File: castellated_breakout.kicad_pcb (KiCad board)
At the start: 2 copper layers, 3 parts, among them J1 Conn_01x14_Female, J2 Conn_01x14_Female, U1 STM32_7x4_Castellated

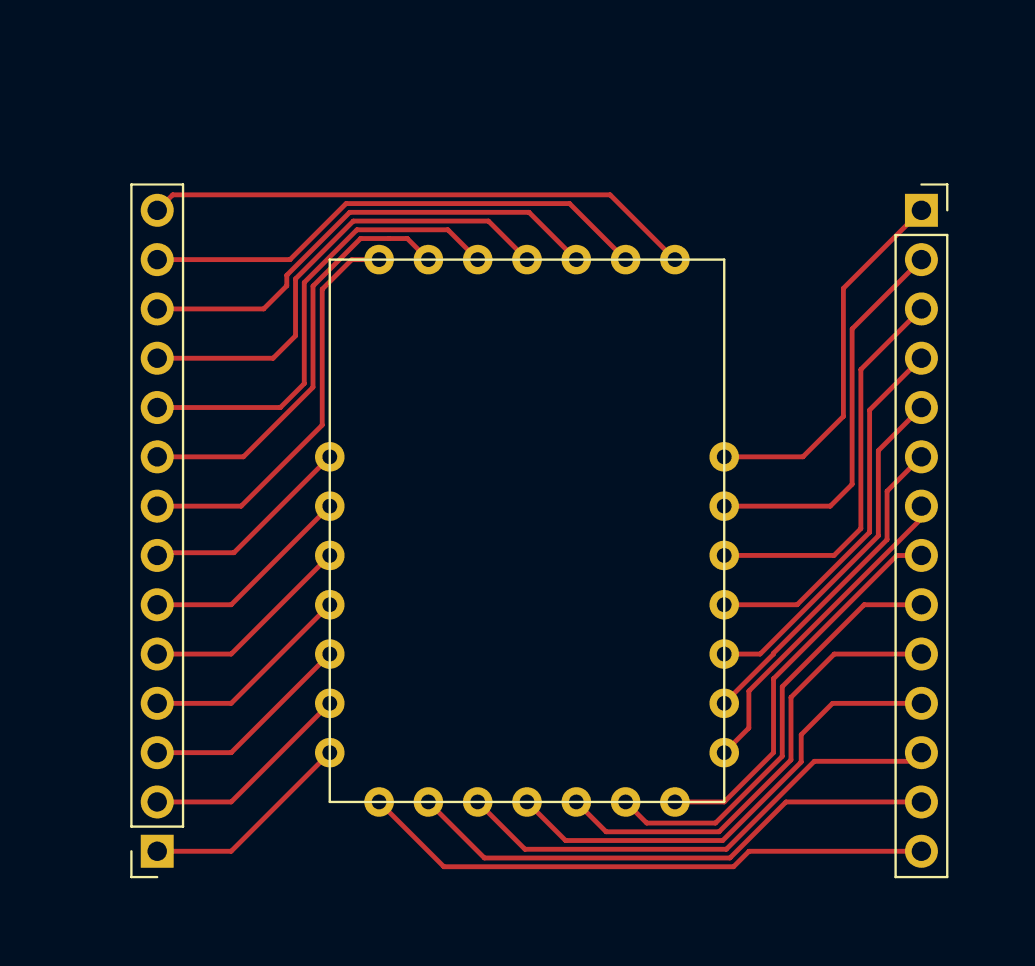
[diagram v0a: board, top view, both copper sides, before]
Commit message: spaced out traces
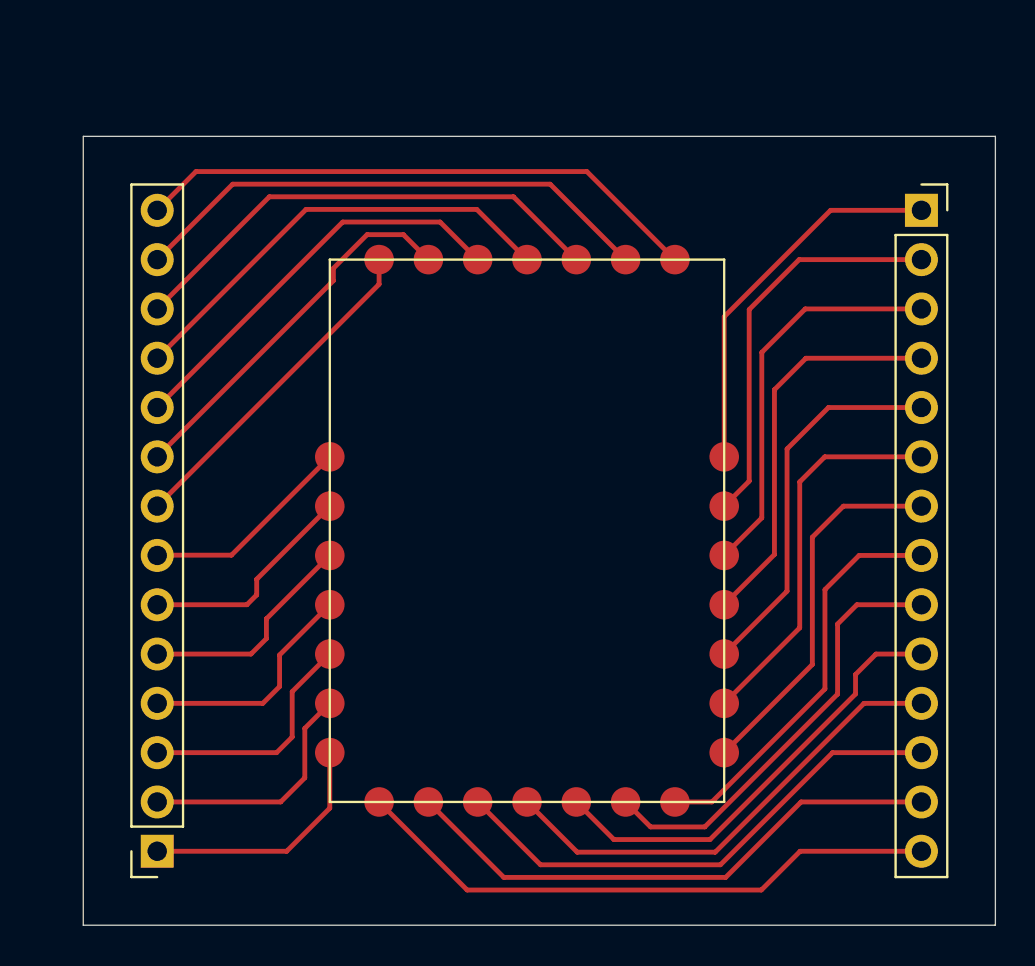
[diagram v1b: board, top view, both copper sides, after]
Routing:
- net Net-(J2-Pad8): track 20.8 -> 17.4 mm
- net Net-(J1-Pad6): track 16.9 -> 19.8 mm
- net Net-(J2-Pad10): track 24.0 -> 21.3 mm
- net Net-(J2-Pad9): track 22.1 -> 19.6 mm
- net Net-(J1-Pad7): track 16.9 -> 19.3 mm
- net Net-(J1-Pad5): track 18.0 -> 19.7 mm
- net Net-(J2-Pad1): track 11.0 -> 12.7 mm
- net Net-(J2-Pad2): track 11.0 -> 12.5 mm
- net Net-(J2-Pad3): track 11.0 -> 12.4 mm
- net Net-(J1-Pad4): track 19.1 -> 20.4 mm
- net Net-(J2-Pad11): track 24.5 -> 23.3 mm
- net Net-(J1-Pad14): track 29.7 -> 30.6 mm
- net Net-(J2-Pad14): track 28.4 -> 29.4 mm
- net Net-(J1-Pad10): track 24.1 -> 23.1 mm
- net Net-(J2-Pad4): track 11.0 -> 11.9 mm
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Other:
- board outline added: 47 x 40.6 mm
- net class Default: clearance 0.2 -> 0.4
- rule trace_clearance: 0.2 -> 0.4

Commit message: gerbers, v1
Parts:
- moved J2 1.91 mm to (137.8, 113.0)
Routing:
- net Net-(J2-Pad7): track 11.0 -> 12.9 mm
- net Net-(J2-Pad9): track 19.6 -> 21.5 mm
- net Net-(J2-Pad8): track 17.4 -> 19.3 mm
- net Net-(J2-Pad6): track 11.5 -> 13.4 mm
- net Net-(J2-Pad5): track 11.6 -> 13.5 mm
- net Net-(J2-Pad4): track 11.9 -> 13.9 mm
- net Net-(J2-Pad3): track 12.4 -> 14.3 mm
- net Net-(J2-Pad2): track 12.5 -> 14.4 mm
- net Net-(J2-Pad14): track 29.4 -> 31.3 mm
- net Net-(J2-Pad13): track 27.4 -> 29.3 mm
- net Net-(J2-Pad12): track 25.3 -> 27.2 mm
- net Net-(J2-Pad11): track 23.3 -> 25.2 mm
- net Net-(J2-Pad10): track 21.3 -> 23.2 mm
- net Net-(J2-Pad1): track 12.7 -> 14.6 mm
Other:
- board size 47 x 40.6 mm -> 48.9 x 40.6 mm
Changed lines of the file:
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@@
   (general
     (thickness 1.6)
-    (drawings 4)
-    (tracks 108)
+    (drawings 6)
+    (tracks 123)
     (zones 0)
     (modules 3)
@@
       (outputformat 1)
       (mirror false)
-      (drillshape 1)
+      (drillshape 0)
       (scaleselection 1)
-      (outputdirectory ""))
+      (outputdirectory "Gerbers/"))
   )
   (net 0 "")
@@
   )
   (module Connector_PinSocket_2.54mm:PinSocket_1x14_P2.54mm_Vertical (layer F.Cu)
-    (at 139.7 113.03 180)
+    (at 137.795 113.03 180)
     (descr "Through hole straight socket strip, 1x14, 2.54mm pitch, single row (from Kicad 4.0.7), script generated")
     (tags "Through hole socket strip THT 1x14 2.54mm single row")
@@
     )
   )
-  (gr_line (start 135.89 116.84) (end 135.89 76.2) (layer Edge.Cuts) (width 0.05))
+  (gr_line (start 133.985 116.84) (end 135.89 116.84) (layer Edge.Cuts) (width 0.05))
+  (gr_line (start 133.985 76.2) (end 135.89 76.2) (layer Edge.Cuts) (width 0.05))
+  (gr_line (start 133.985 116.84) (end 133.985 76.2) (layer Edge.Cuts) (width 0.05))
   (gr_line (start 182.88 116.84) (end 135.89 116.84) (layer Edge.Cuts) (width 0.05))
   (gr_line (start 182.88 76.2) (end 182.88 116.84) (layer Edge.Cuts) (width 0.05))
@@
   (segment (start 161.832949 78.012949) (end 141.697051 78.012949) (width 0.25) (layer F.Cu) (net 15))
   (segment (start 166.37 82.55) (end 161.832949 78.012949) (width 0.25) (layer F.Cu) (net 15))
+  (segment (start 139.7 80.01) (end 137.795 80.01) (width 0.25) (layer F.Cu) (net 15))
   (segment (start 159.942959 78.662959) (end 143.587041 78.662959) (width 0.25) (layer F.Cu) (net 16))
   (segment (start 143.587041 78.662959) (end 139.7 82.55) (width 0.25) (layer F.Cu) (net 16))
   (segment (start 163.83 82.55) (end 159.942959 78.662959) (width 0.25) (layer F.Cu) (net 16))
+  (segment (start 139.7 82.55) (end 137.795 82.55) (width 0.25) (layer F.Cu) (net 16))
   (segment (start 145.477031 79.312969) (end 139.7 85.09) (width 0.25) (layer F.Cu) (net 17))
   (segment (start 158.052969 79.312969) (end 145.477031 79.312969) (width 0.25) (layer F.Cu) (net 17))
   (segment (start 161.29 82.55) (end 158.052969 79.312969) (width 0.25) (layer F.Cu) (net 17))
+  (segment (start 139.7 85.09) (end 137.795 85.09) (width 0.25) (layer F.Cu) (net 17))
   (segment (start 147.367021 79.962979) (end 139.7 87.63) (width 0.25) (layer F.Cu) (net 18))
   (segment (start 156.162979 79.962979) (end 147.367021 79.962979) (width 0.25) (layer F.Cu) (net 18))
   (segment (start 158.75 82.55) (end 156.162979 79.962979) (width 0.25) (layer F.Cu) (net 18))
+  (segment (start 139.7 87.63) (end 137.795 87.63) (width 0.25) (layer F.Cu) (net 18))
   (segment (start 149.257011 80.612989) (end 139.7 90.17) (width 0.25) (layer F.Cu) (net 19))
   (segment (start 154.272989 80.612989) (end 149.257011 80.612989) (width 0.25) (layer F.Cu) (net 19))
   (segment (start 156.21 82.55) (end 154.272989 80.612989) (width 0.25) (layer F.Cu) (net 19))
+  (segment (start 139.7 90.17) (end 137.795 90.17) (width 0.25) (layer F.Cu) (net 19))
   (segment (start 150.512239 81.262999) (end 148.775 83.000238) (width 0.25) (layer F.Cu) (net 20))
   (segment (start 152.382999 81.262999) (end 150.512239 81.262999) (width 0.25) (layer F.Cu) (net 20))
@@
   (segment (start 148.775 83.635) (end 139.7 92.71) (width 0.25) (layer F.Cu) (net 20))
   (segment (start 148.775 83.000238) (end 148.775 83.635) (width 0.25) (layer F.Cu) (net 20))
+  (segment (start 139.7 92.71) (end 137.795 92.71) (width 0.25) (layer F.Cu) (net 20))
   (segment (start 151.13 83.82) (end 139.7 95.25) (width 0.25) (layer F.Cu) (net 21))
   (segment (start 151.13 82.55) (end 151.13 83.82) (width 0.25) (layer F.Cu) (net 21))
+  (segment (start 139.7 95.25) (end 137.795 95.25) (width 0.25) (layer F.Cu) (net 21))
   (segment (start 148.59 92.71) (end 143.525 97.775) (width 0.25) (layer F.Cu) (net 22))
   (segment (start 139.715 97.775) (end 139.7 97.79) (width 0.25) (layer F.Cu) (net 22))
   (segment (start 143.525 97.775) (end 139.715 97.775) (width 0.25) (layer F.Cu) (net 22))
+  (segment (start 137.81 97.775) (end 137.795 97.79) (width 0.25) (layer F.Cu) (net 22))
+  (segment (start 139.715 97.775) (end 137.81 97.775) (width 0.25) (layer F.Cu) (net 22))
   (segment (start 148.59 95.25) (end 144.825 99.015) (width 0.25) (layer F.Cu) (net 23))
   (segment (start 144.825 99.015) (end 144.825 99.825) (width 0.25) (layer F.Cu) (net 23))
   (segment (start 144.32 100.33) (end 139.7 100.33) (width 0.25) (layer F.Cu) (net 23))
   (segment (start 144.825 99.825) (end 144.32 100.33) (width 0.25) (layer F.Cu) (net 23))
+  (segment (start 139.7 100.33) (end 137.795 100.33) (width 0.25) (layer F.Cu) (net 23))
   (segment (start 148.59 97.79) (end 145.325 101.055) (width 0.25) (layer F.Cu) (net 24))
   (segment (start 145.325 101.055) (end 145.325 102.075) (width 0.25) (layer F.Cu) (net 24))
   (segment (start 144.53 102.87) (end 139.7 102.87) (width 0.25) (layer F.Cu) (net 24))
   (segment (start 145.325 102.075) (end 144.53 102.87) (width 0.25) (layer F.Cu) (net 24))
+  (segment (start 139.7 102.87) (end 137.795 102.87) (width 0.25) (layer F.Cu) (net 24))
   (segment (start 148.59 100.33) (end 146.002981 102.917019) (width 0.25) (layer F.Cu) (net 25))
   (segment (start 146.002981 102.917019) (end 146.002981 104.547019) (width 0.25) (layer F.Cu) (net 25))
   (segment (start 145.14 105.41) (end 139.7 105.41) (width 0.25) (layer F.Cu) (net 25))
   (segment (start 146.002981 104.547019) (end 145.14 105.41) (width 0.25) (layer F.Cu) (net 25))
+  (segment (start 139.7 105.41) (end 137.795 105.41) (width 0.25) (layer F.Cu) (net 25))
   (segment (start 148.59 102.87) (end 146.652989 104.807011) (width 0.25) (layer F.Cu) (net 26))
   (segment (start 146.652989 104.807011) (end 146.652989 107.147011) (width 0.25) (layer F.Cu) (net 26))
   (segment (start 145.85 107.95) (end 139.7 107.95) (width 0.25) (layer F.Cu) (net 26))
   (segment (start 146.652989 107.147011) (end 145.85 107.95) (width 0.25) (layer F.Cu) (net 26))
+  (segment (start 139.7 107.95) (end 137.795 107.95) (width 0.25) (layer F.Cu) (net 26))
   (segment (start 147.302999 106.697001) (end 147.302999 109.247001) (width 0.25) (layer F.Cu) (net 27))
   (segment (start 148.59 105.41) (end 147.302999 106.697001) (width 0.25) (layer F.Cu) (net 27))
   (segment (start 146.06 110.49) (end 139.7 110.49) (width 0.25) (layer F.Cu) (net 27))
   (segment (start 147.302999 109.247001) (end 146.06 110.49) (width 0.25) (layer F.Cu) (net 27))
+  (segment (start 139.7 110.49) (end 137.795 110.49) (width 0.25) (layer F.Cu) (net 27))
   (segment (start 148.59 107.95) (end 148.59 110.81) (width 0.25) (layer F.Cu) (net 28))
   (segment (start 146.37 113.03) (end 139.7 113.03) (width 0.25) (layer F.Cu) (net 28))
   (segment (start 148.59 110.81) (end 146.37 113.03) (width 0.25) (layer F.Cu) (net 28))
+  (segment (start 139.7 113.03) (end 137.795 113.03) (width 0.25) (layer F.Cu) (net 28))
 )

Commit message: v2 voltera, v1 pcbway
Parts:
- added G***: LOGO, trylaarsdam:wcl_logo, F.Cu at (157.9, 114.8)
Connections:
- net Net-(J1-Pad1) renamed SPI_MISO
- net Net-(J1-Pad10) renamed SWO
- net Net-(J1-Pad11) renamed TX_1
- net Net-(J1-Pad12) renamed DEBUG_JRST
- net Net-(J1-Pad13) renamed JTDI
- net Net-(J1-Pad14) renamed SWCLK
- net Net-(J1-Pad2) renamed PA5
- net Net-(J1-Pad3) renamed VCP_RX
- net Net-(J1-Pad4) renamed VCP_TX
- net Net-(J1-Pad5) renamed SPI_CLK
- net Net-(J1-Pad6) renamed PWR_WKUP
- net Net-(J1-Pad7) renamed SCL
- net Net-(J1-Pad8) renamed SDA
- net Net-(J1-Pad9) renamed SPI_MOSI
- net Net-(J2-Pad1) renamed VBAT
- net Net-(J2-Pad10) renamed GND
- net Net-(J2-Pad11) renamed RF2
- net Net-(J2-Pad12) renamed RF3
- net Net-(J2-Pad13) renamed BOOT0
- net Net-(J2-Pad14) renamed RST
- net Net-(J2-Pad2) renamed SWDIO
- net Net-(J2-Pad3) renamed PA12
- net Net-(J2-Pad4) renamed PA11
- net Net-(J2-Pad5) renamed RX_1
- net Net-(J2-Pad6) renamed PB12
- net Net-(J2-Pad7) renamed PB2
- net Net-(J2-Pad8) renamed VDD
- net Net-(J2-Pad9) renamed RF1V55
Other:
- board text added: "BOOT0"
- board text added: "DBG_JRST"
- board text added: "GND"
- board text added: "JTDI"
- board text added: "PA11"
- board text added: "PA12"
- board text added: "PA5"
- board text added: "PB12"
- board text added: "PB2"
- board text added: "RF1V55"
- board text added: "RF2"
- board text added: "RF3"
- board text added: "RST"
- board text added: "RX_1"
- board text added: "SCL"
- board text added: "SDA"
- board text added: "SPI_CLK"
- board text added: "SPI_MISO"
- board text added: "SPI_MOSI"
- board text added: "SWCLK"
- board text added: "SWDIO"
- board text added: "SWO"
- board text added: "TX_1"
- board text added: "VBAT"
- board text added: "VCP_RX"
- board text added: "VCP_TX"
- board text added: "VDD"
- board text added: "WKUP"
- board text added: "v1.0.0"

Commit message: v2 pcbway
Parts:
- added SWD: Conn_01x06_Female, Connector:Tag-Connect_TC2030-IDC-NL_2x03_P1.27mm_Vertical, F.Cu at (166.1, 78.8)
- moved G*** 9.94 mm to (148.0, 114.2)
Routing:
- net SWDIO: track 14.4 -> 66.4 mm, vias 0 -> 2
- net SWCLK: track 30.6 -> 79.6 mm, vias 0 -> 2
- net SWO: track 23.1 -> 55.0 mm, vias 0 -> 1
- net VDD: track 19.3 -> 36.3 mm, vias 0 -> 2
- net GND: track 23.2 -> 39.2 mm
- net RST: track 31.3 -> 34.0 mm, vias 0 -> 2
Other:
- outline, holes or cut-outs redrawn
- board text added: "v1.1.0"
- board text removed: "v1.0.0"

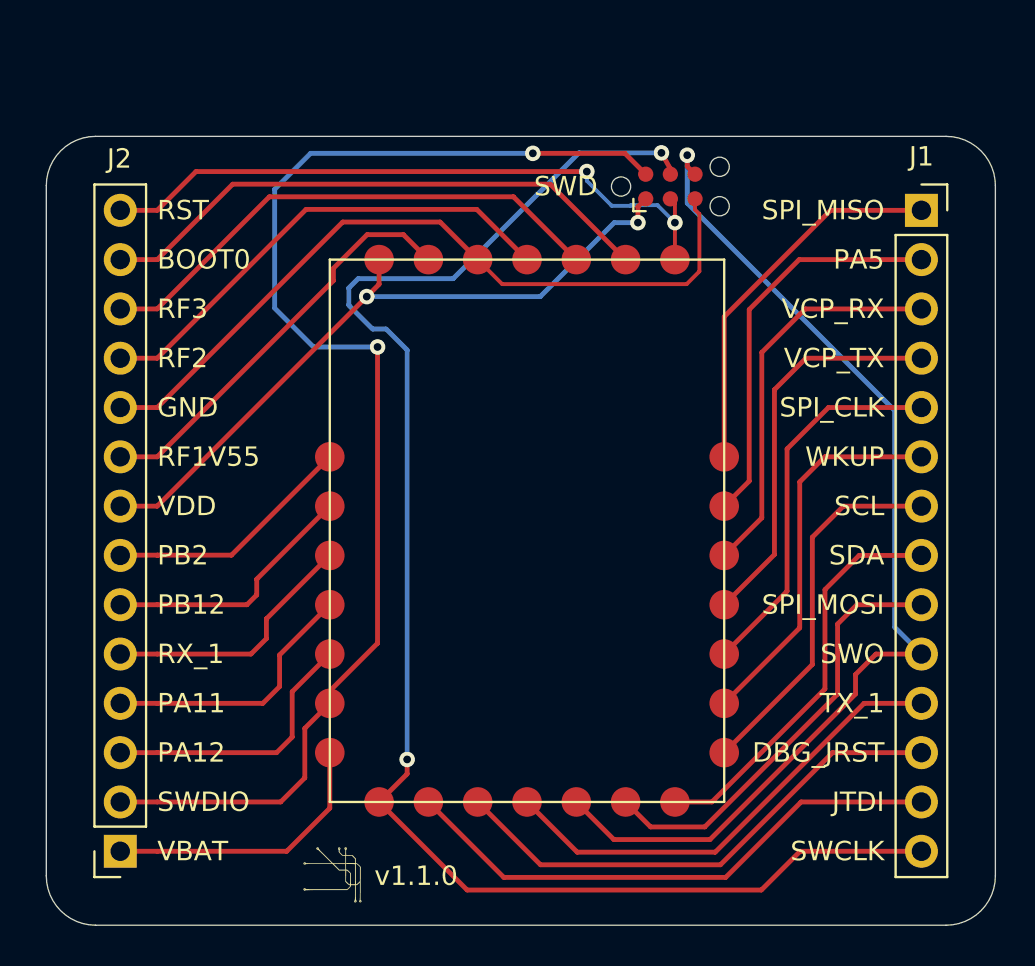
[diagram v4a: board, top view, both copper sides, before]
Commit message: locking tag connect
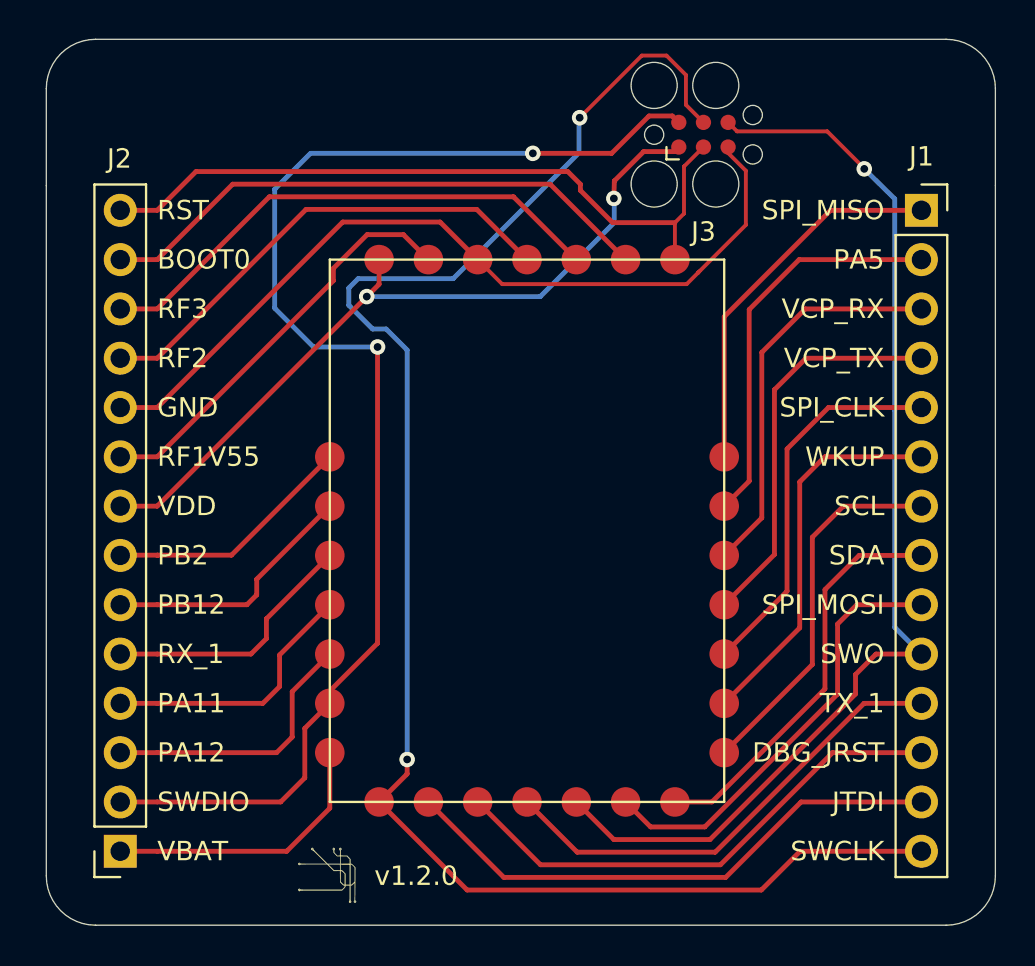
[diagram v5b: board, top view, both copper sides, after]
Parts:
- J3: renamed from SWD; footprint Connector:Tag-Connect_TC2030-IDC-NL_2x03_P1.27mm_Vertical -> Connector:Tag-Connect_TC2030-IDC-FP_2x03_P1.27mm_Vertical
- moved J3 3.17 mm to (167.8, 76.1)
- moved G*** 0.28 mm to (147.7, 114.3)
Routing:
- net SWCLK: track 79.6 -> 86.0 mm
- net GND: track 39.2 -> 43.3 mm
- net VDD: track 36.3 -> 39.9 mm
- net RST: track 34.0 -> 37.1 mm, vias 2 -> 0
- net SWO: track 55.0 -> 57.4 mm
- net SWDIO: track 66.4 -> 68.6 mm
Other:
- board size 48.9 x 40.6 mm -> 48.9 x 45.6 mm
- net class Default removed
- board text added: "v1.2.0"
- board text removed: "v1.1.0"

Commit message: updates
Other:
- board text added: "v1.2.1"
- board text removed: "v1.2.0"
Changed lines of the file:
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@@
       (disableapertmacros false)
       (usegerberextensions false)
-      (usegerberattributes true)
+      (usegerberattributes false)
       (usegerberadvancedattributes true)
       (creategerberjobfile true)
@@
     (effects (font (size 1 1) (thickness 0.15)) (justify right))
   )
-  (gr_text "v1.2.0" (at 153.035 114.3) (layer "F.SilkS")
+  (gr_text "v1.2.1" (at 153.035 114.3) (layer "F.SilkS")
     (effects (font (size 1 1) (thickness 0.15)))
   )
